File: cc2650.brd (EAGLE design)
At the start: 50.8 x 22.9 mm, 24 parts, among them IC1 TPS73133DBVR, IC4 CC2650MODAMOHR, SW1 SPST_TACT-KMR2, SW3 SPST_TACT-KMR2, U1 Value

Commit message: changed resistors and LEDs to 0603, capacitors to 0805.
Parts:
- removed LED2: GREEN, adafruit:CHIPLED_1206
- removed R2: 715, adafruit:R1206
- added LED0: RED, adafruit:CHIPLED_0603
- C2: value 0.1u -> 1n; device adafruit:C1206 -> adafruit:C0805
- C3: value 1n -> 100n; device adafruit:C1206 -> adafruit:C0805
- LED1: value RED -> GREEN; device adafruit:CHIPLED_1206 -> adafruit:CHIPLED_0603
- R1: device adafruit:R1206 -> adafruit:R0603
- R3: value 787 -> 715; device adafruit:R1206 -> adafruit:R0603
- R5: value 47k -> 787; device adafruit:R1206 -> adafruit:R0603
- R7: value 715 -> 47k; device adafruit:R1206 -> adafruit:R0603
- moved R7 26.3 mm to (6.99, 5.08), turned to 180 degrees
- moved C1 18.1 mm to (10.7, 7.43), turned to 180 degrees
- moved C3 14.6 mm to (10.2, 15.2), flipped to the top, turned to 0 degrees
- moved C2 14.5 mm to (2.54, 3.17), flipped to the bottom, turned to 90 degrees
- moved R5 13.5 mm to (17.8, 12.7), flipped to the bottom, turned to 90 degrees
- moved LED1 3.01 mm to (20.6, 12.7), turned to 180 degrees
- moved R3 3.01 mm to (20.6, 12.7), turned to 90 degrees
- moved R6 2.84 mm to (26.0, 19.1)
- moved U1 2.54 mm to (15.4, 6.03)
- moved SW3 2.54 mm to (19.2, 9.53)
- moved R1 1.76 mm to (5.71, 17.8)
- moved R4 1.42 mm to (26.0, 17.1), flipped to the top, turned to 180 degrees
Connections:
- net GND: now also LED0.C; no longer LED2.C
- net GPIO_LED: now also LED1.A, R3.1; no longer LED2.A, R2.2
- net GPIO_LED_JPR: now also R3.2; no longer R2.1
- net NRESET: now also C2.1, R7.2; no longer C3.1, R5.2
- net PWR_LED: now also LED0.A, R5.1; no longer LED1.A, R3.2
- net PWR_LED_JPR: now also R5.2; no longer R3.1
- net VBUS: now also C3.1; no longer C2.1
- net VCC: now also R7.1; no longer R5.1
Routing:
- net VCC: track 92.6 -> 74.7 mm
- net VBUS: track 29.7 -> 23.9 mm
- net GPIO_LED: track 4.71 -> 0.00 mm, vias 1 -> 0
- net PWR_LED: track 4.27 -> 0.00 mm, vias 1 -> 0
- net PWR_LED_JPR: track 2.64 -> 0.00 mm
- net GPIO_LED_JPR: track 2.64 -> 0.00 mm
- net DIO14: track 29.1 -> 30.3 mm
- net NRESET: track 53.6 -> 54.5 mm

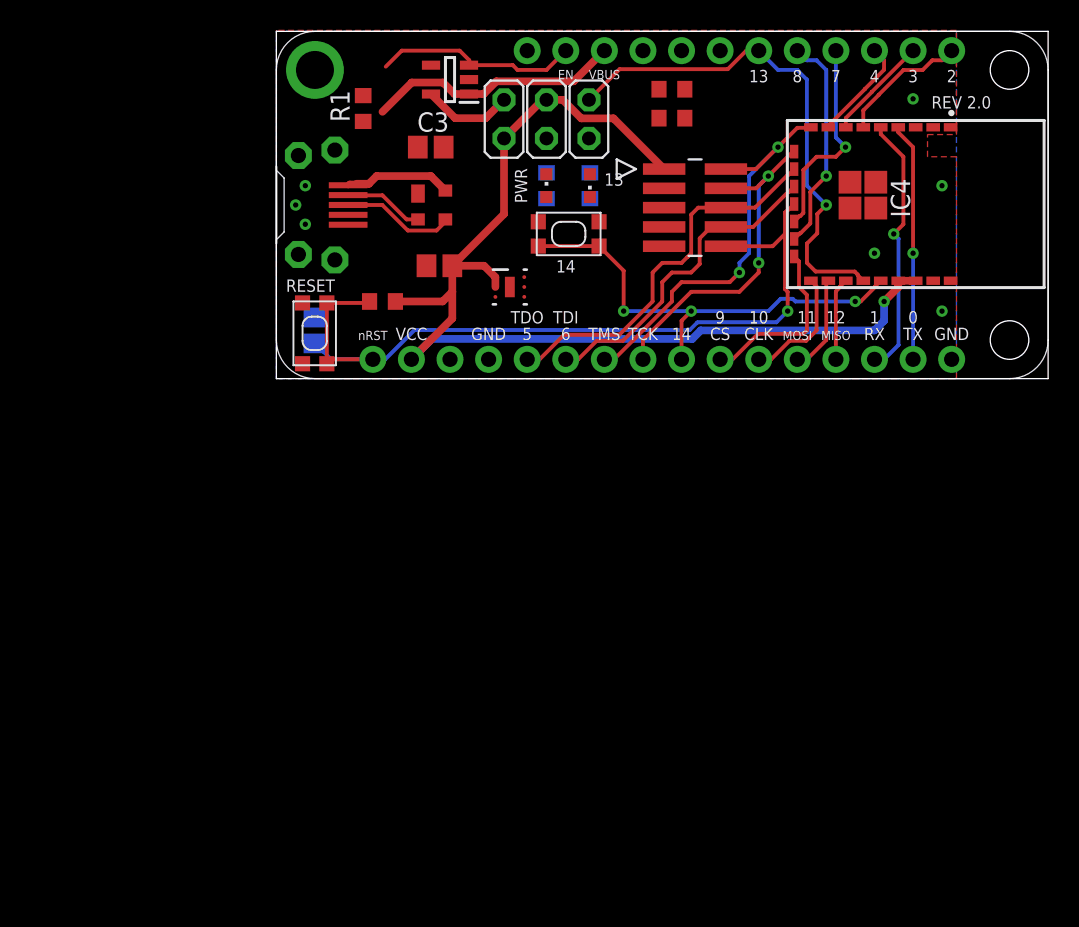
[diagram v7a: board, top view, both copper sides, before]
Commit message: tweaked some component positions.
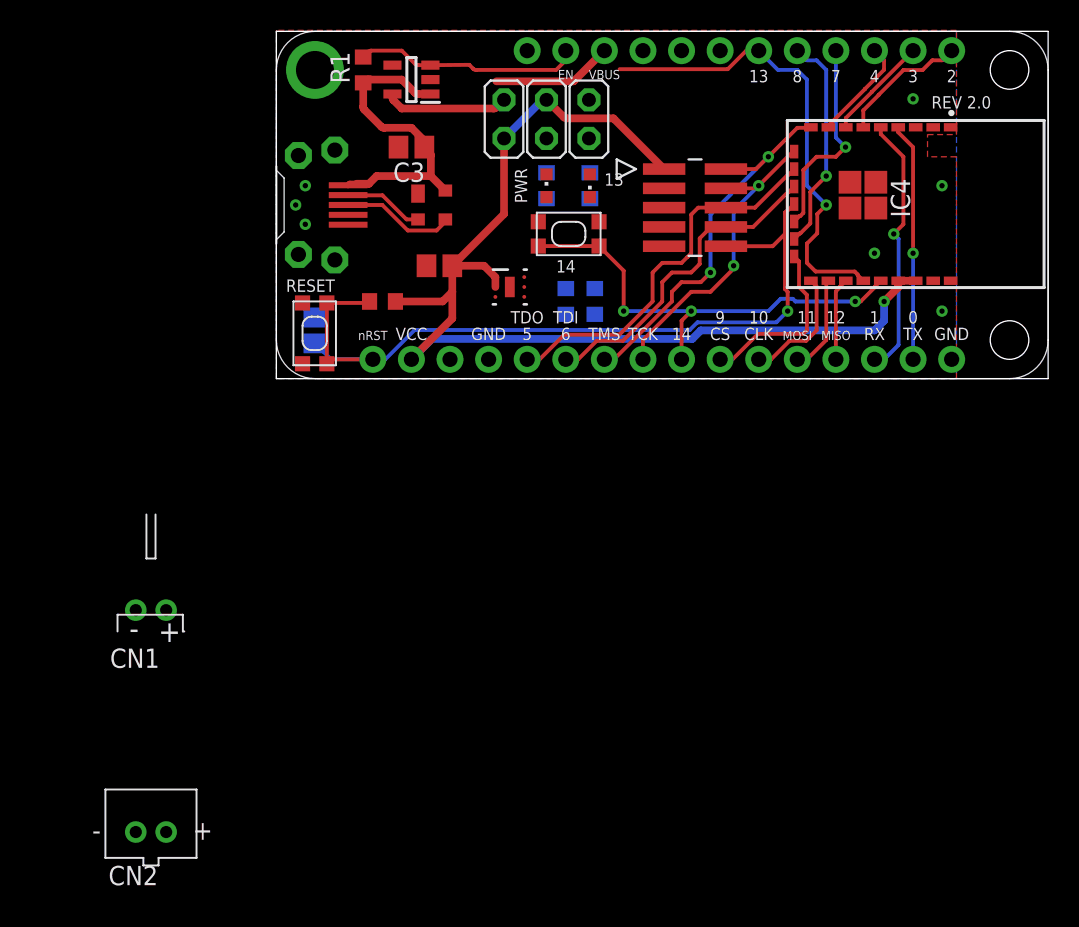
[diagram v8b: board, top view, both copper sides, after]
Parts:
- added CN1: (no value), wing_modified:JST-PH-2-THM-RA
- added CN2: (no value), wing_modified:JST-PH-2-THM
- moved R6 14.9 mm to (21.0, 5.08), flipped to the bottom, turned to 270 degrees
- moved R4 13.9 mm to (19.1, 5.08), flipped to the bottom, turned to 270 degrees
- moved IC1 2.54 mm to (8.89, 19.7)
- moved R1 2.54 mm to (5.71, 20.3)
- moved C3 1.27 mm to (8.89, 15.2), turned to 180 degrees
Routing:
- net VBUS: track 23.9 -> 28.9 mm
- net DIO13: track 33.8 -> 31.0 mm
- net VCC_JPR: track 5.96 -> 8.15 mm
- net JTAG_TMS: track 27.7 -> 25.7 mm
- net JTAG_TCK: track 23.0 -> 21.0 mm
- net EN: track 13.6 -> 14.9 mm
